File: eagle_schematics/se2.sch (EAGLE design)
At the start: 8 parts, among them J1 MAGJACK-NOLABELS

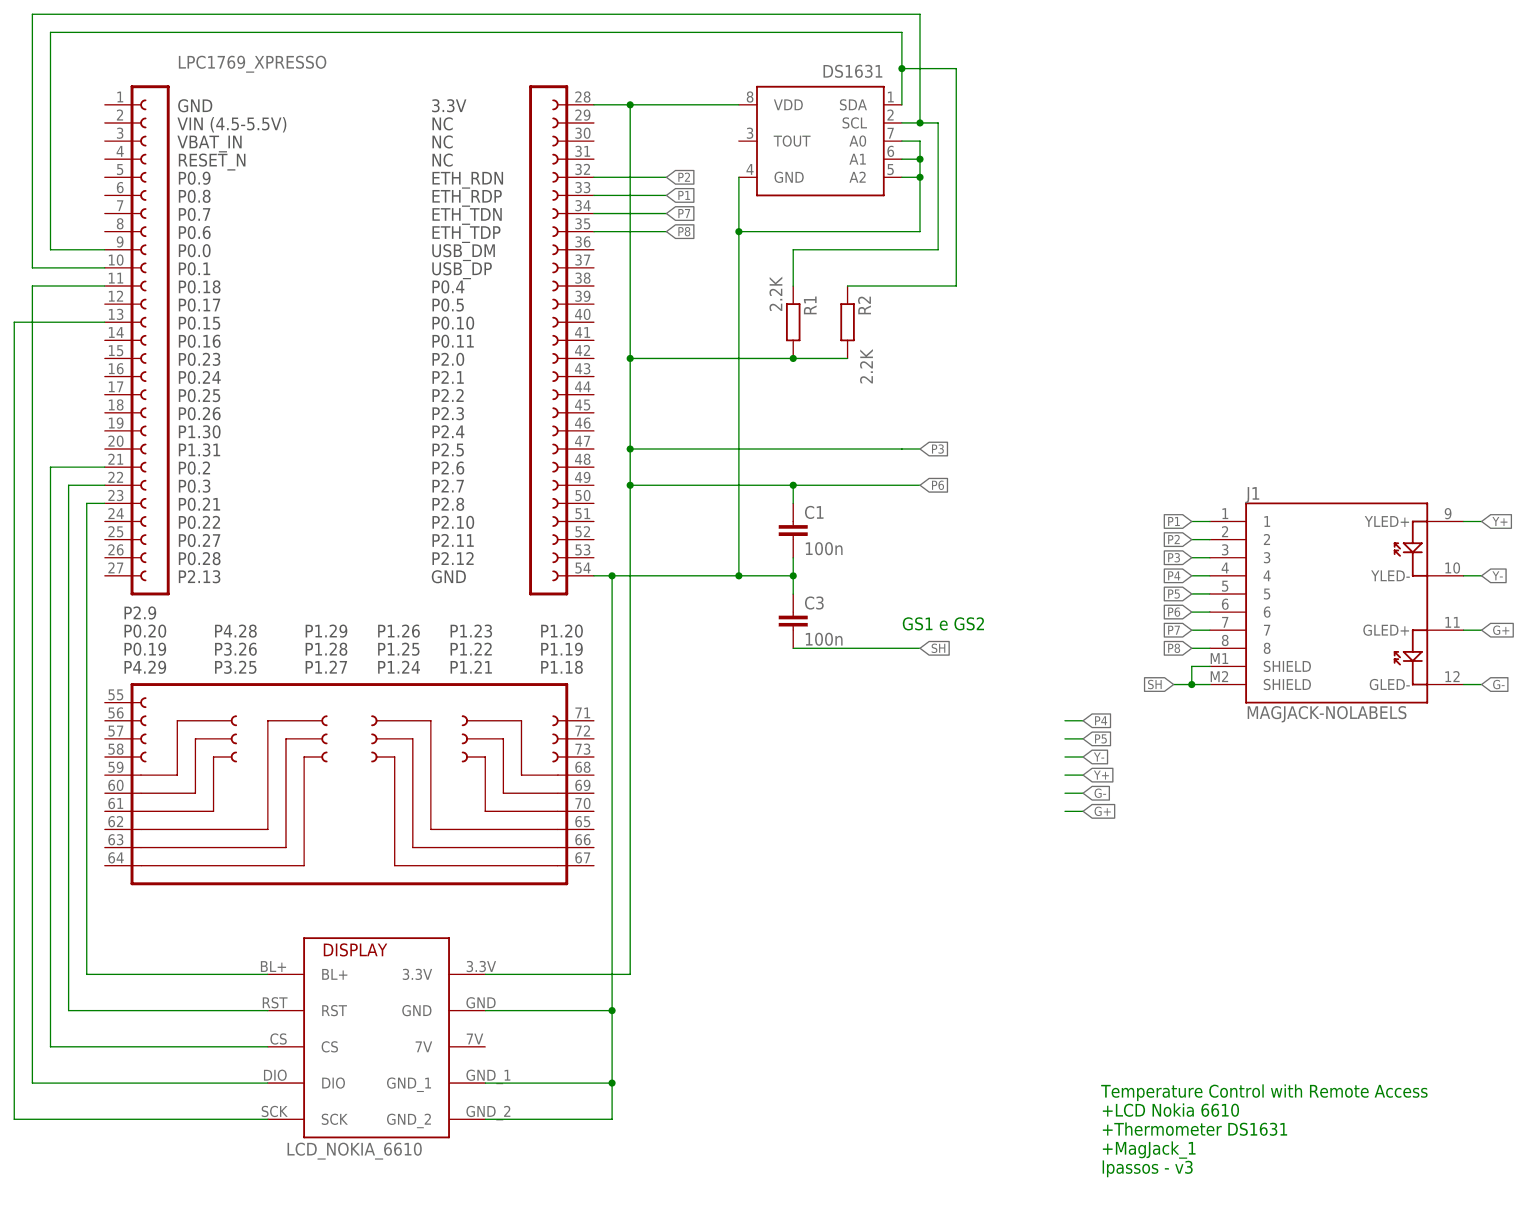
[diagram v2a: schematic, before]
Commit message: led schematic added
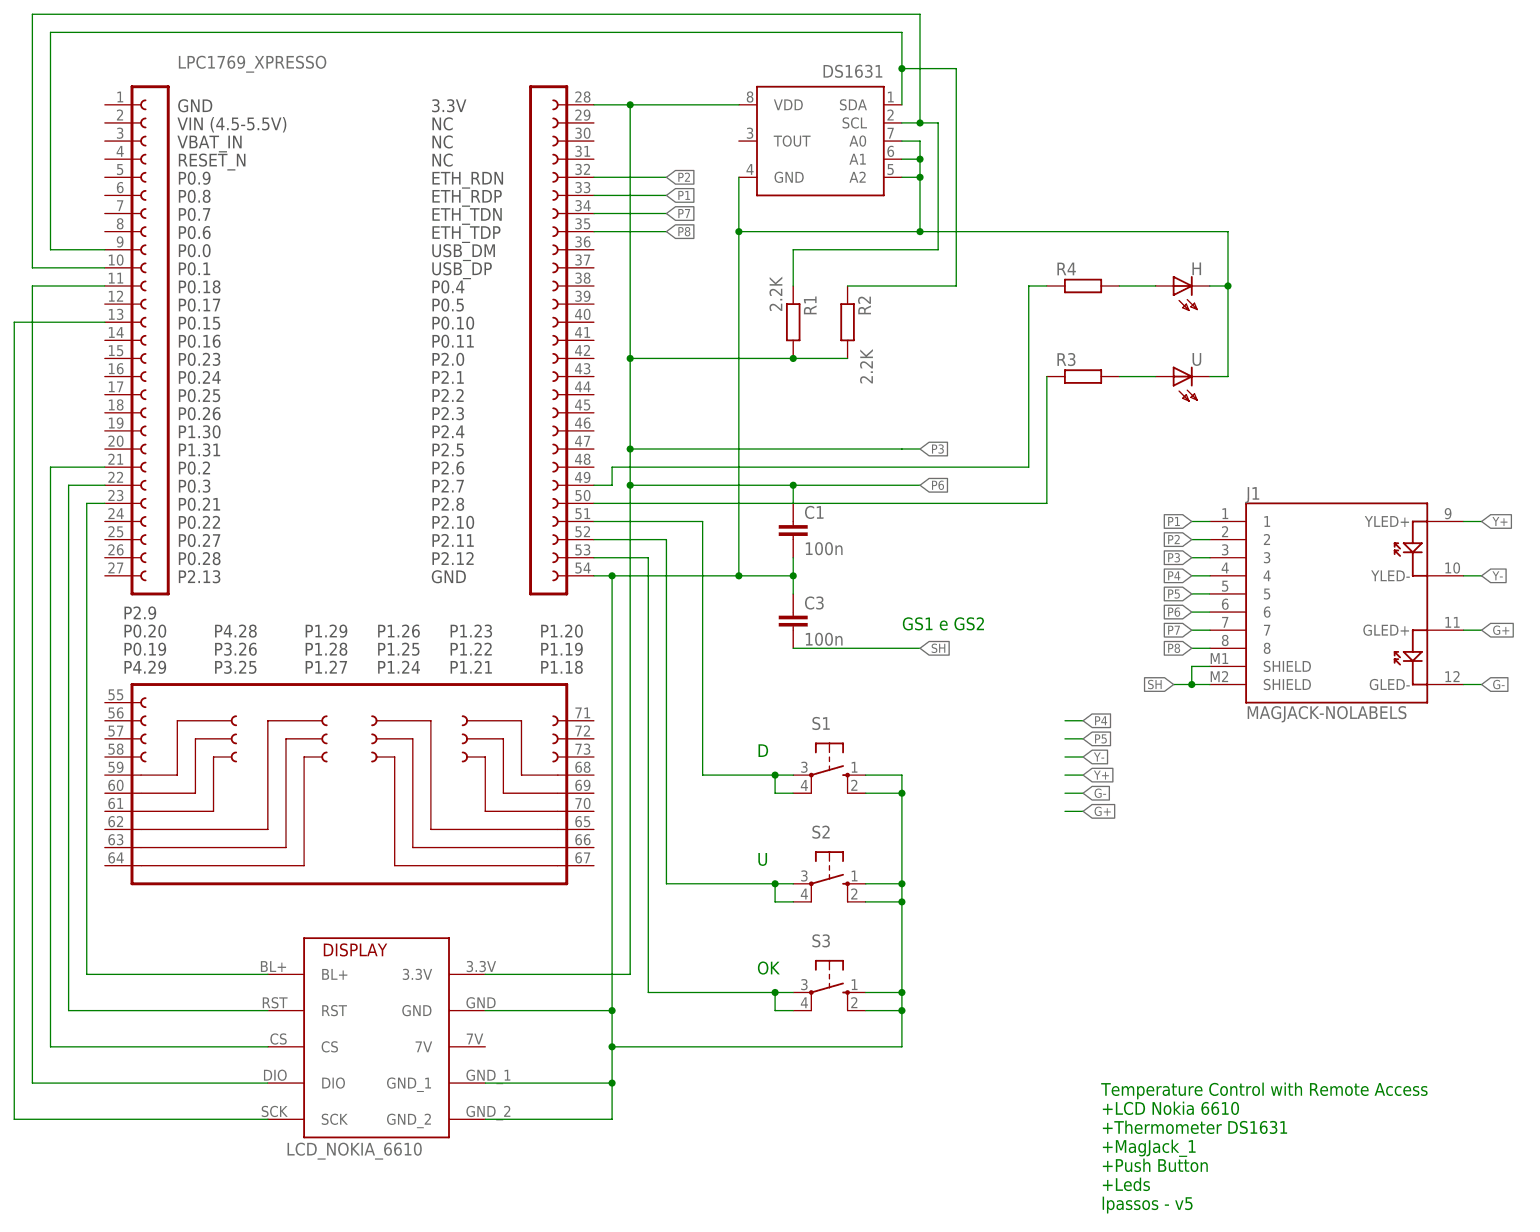
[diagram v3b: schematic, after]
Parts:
- added H, U: HLMP6, display-hp:HLMP6
- added R3, R4: (no value), eagle-ltspice:R
- added S1, S2, S3: (no value), switch-omron:10-XX
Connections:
- new net N$1: LPC1769_XPRESSO.51, S1.P, S1.P1
- new net N$12: LPC1769_XPRESSO.52, S2.P, S2.P1
- new net N$13: R3.2, U.A
- new net N$14: LPC1769_XPRESSO.50, R3.1
- new net N$15: LPC1769_XPRESSO.49, R4.1
- new net N$2: LPC1769_XPRESSO.53, S3.P, S3.P1
- new net N$3: H.A, R4.2
- net N$9: now also H.K, S1.S, S1.S1, S2.S, S2.S1, S3.S, S3.S1, U.K
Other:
- note added: "D"
- note added: "OK"
- note added: "Temperature Control with Remote Access +LCD Nokia 6610 +Thermometer DS1631 +MagJack_1 +Push Button +Leds lpassos - v5"
- note added: "U"
- note removed: "Temperature Control with Remote Access +LCD Nokia 6610 +Thermometer DS1631 +MagJack_1 lpassos - v3"
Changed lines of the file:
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@@
 <setting verticaltext="up"/>
 </settings>
-<grid distance="0.1" unitdist="inch" unit="inch" style="lines" multiple="1" display="no" altdistance="0.01" altunitdist="inch" altunit="inch"/>
+<grid distance="0.1" unitdist="inch" unit="inch" style="lines" multiple="1" display="yes" altdistance="0.01" altunitdist="inch" altunit="inch"/>
 <layers>
 <layer number="1" name="Top" color="4" fill="1" visible="no" active="no"/>
@@
 <part name="C1" library="capacitor-wima" deviceset="C" device="2,5-3" value="100n"/>
 <part name="C3" library="capacitor-wima" deviceset="C" device="2,5-3" value="100n"/>
+<part name="S1" library="switch-omron" deviceset="10-XX" device=""/>
+<part name="S2" library="switch-omron" deviceset="10-XX" device=""/>
+<part name="S3" library="switch-omron" deviceset="10-XX" device=""/>
+<part name="R3" library="eagle-ltspice" deviceset="R" device=""/>
+<part name="R4" library="eagle-ltspice" deviceset="R" device=""/>
+<part name="H" library="display-hp" deviceset="HLMP6" device="" value=""/>
+<part name="U" library="display-hp" deviceset="HLMP6" device="" value=""/>
 </parts>
 <sheets>
 <sheet>
 <plain>
-<text x="182.88" y="93.98" size="1.778" layer="91">Temperature Control with Remote Access
+<text x="182.88" y="88.9" size="1.778" layer="91">Temperature Control with Remote Access
 +LCD Nokia 6610
 +Thermometer DS1631
 +MagJack_1
-lpassos - v3</text>
++Push Button
++Leds
+lpassos - v5</text>
 <text x="154.94" y="170.18" size="1.778" layer="91">GS1 e GS2</text>
+<text x="134.62" y="121.92" size="1.778" layer="91">OK</text>
+<text x="134.62" y="137.16" size="1.778" layer="91">U</text>
+<text x="134.62" y="152.4" size="1.778" layer="91">D</text>
 </plain>
 <instances>
@@
 <instance part="C1" gate="G$1" x="139.7" y="185.42"/>
 <instance part="C3" gate="G$1" x="139.7" y="172.72"/>
+<instance part="S1" gate="1" x="144.78" y="149.86" rot="R270"/>
+<instance part="S2" gate="1" x="144.78" y="134.62" rot="R270"/>
+<instance part="S3" gate="1" x="144.78" y="119.38" rot="R270"/>
+<instance part="R3" gate="G$1" x="180.34" y="205.74"/>
+<instance part="R4" gate="G$1" x="180.34" y="218.44"/>
+<instance part="H" gate="A" x="195.58" y="218.44" rot="R90"/>
+<instance part="U" gate="A" x="195.58" y="205.74" rot="R90"/>
 </instances>
 <busses>
@@
 <pinref part="DISPLAY" gate="G$1" pin="GND_1"/>
 <wire x1="96.52" y1="106.68" x2="114.3" y2="106.68" width="0.1524" layer="91"/>
-<wire x1="114.3" y1="106.68" x2="114.3" y2="116.84" width="0.1524" layer="91"/>
+<wire x1="114.3" y1="106.68" x2="114.3" y2="111.76" width="0.1524" layer="91"/>
 <pinref part="DISPLAY" gate="G$1" pin="GND_2"/>
+<wire x1="114.3" y1="111.76" x2="114.3" y2="116.84" width="0.1524" layer="91"/>
 <wire x1="96.52" y1="101.6" x2="114.3" y2="101.6" width="0.1524" layer="91"/>
 <wire x1="114.3" y1="101.6" x2="114.3" y2="106.68" width="0.1524" layer="91"/>
@@
 <pinref part="C3" gate="G$1" pin="1"/>
 <wire x1="139.7" y1="175.26" x2="139.7" y2="177.8" width="0.1524" layer="91"/>
+<wire x1="154.94" y1="147.32" x2="154.94" y2="134.62" width="0.1524" layer="91"/>
+<wire x1="154.94" y1="134.62" x2="154.94" y2="132.08" width="0.1524" layer="91"/>
+<wire x1="154.94" y1="132.08" x2="154.94" y2="119.38" width="0.1524" layer="91"/>
+<wire x1="154.94" y1="119.38" x2="154.94" y2="116.84" width="0.1524" layer="91"/>
+<wire x1="154.94" y1="116.84" x2="154.94" y2="111.76" width="0.1524" layer="91"/>
+<wire x1="154.94" y1="111.76" x2="114.3" y2="111.76" width="0.1524" layer="91"/>
+<junction x="114.3" y="111.76"/>
+<pinref part="S1" gate="1" pin="S1"/>
+<wire x1="149.86" y1="147.32" x2="154.94" y2="147.32" width="0.1524" layer="91"/>
+<pinref part="S3" gate="1" pin="S1"/>
+<wire x1="149.86" y1="116.84" x2="154.94" y2="116.84" width="0.1524" layer="91"/>
+<junction x="154.94" y="116.84"/>
+<pinref part="S2" gate="1" pin="S1"/>
+<wire x1="149.86" y1="132.08" x2="154.94" y2="132.08" width="0.1524" layer="91"/>
+<junction x="154.94" y="132.08"/>
+<pinref part="S1" gate="1" pin="S"/>
+<wire x1="149.86" y1="149.86" x2="154.94" y2="149.86" width="0.1524" layer="91"/>
+<wire x1="154.94" y1="149.86" x2="154.94" y2="147.32" width="0.1524" layer="91"/>
+<pinref part="S2" gate="1" pin="S"/>
+<wire x1="149.86" y1="134.62" x2="154.94" y2="134.62" width="0.1524" layer="91"/>
+<pinref part="S3" gate="1" pin="S"/>
+<wire x1="149.86" y1="119.38" x2="154.94" y2="119.38" width="0.1524" layer="91"/>
+<junction x="154.94" y="147.32"/>
+<junction x="154.94" y="134.62"/>
+<junction x="154.94" y="119.38"/>
+<pinref part="H" gate="A" pin="K"/>
+<wire x1="198.12" y1="218.44" x2="200.66" y2="218.44" width="0.1524" layer="91"/>
+<wire x1="200.66" y1="218.44" x2="200.66" y2="205.74" width="0.1524" layer="91"/>
+<pinref part="U" gate="A" pin="K"/>
+<wire x1="200.66" y1="205.74" x2="198.12" y2="205.74" width="0.1524" layer="91"/>
+<wire x1="157.48" y1="226.06" x2="200.66" y2="226.06" width="0.1524" layer="91"/>
+<wire x1="200.66" y1="226.06" x2="200.66" y2="218.44" width="0.1524" layer="91"/>
+<junction x="200.66" y="218.44"/>
+<junction x="157.48" y="226.06"/>
 </segment>
 </net>
@@
 </segment>
 </net>
+<net name="N$2" class="0">
+<segment>
+<pinref part="LPC1769_XPRESSO" gate="G$1" pin="53"/>
+<wire x1="111.76" y1="180.34" x2="119.38" y2="180.34" width="0.1524" layer="91"/>
+<wire x1="119.38" y1="180.34" x2="119.38" y2="119.38" width="0.1524" layer="91"/>
+<pinref part="S3" gate="1" pin="P"/>
+<wire x1="119.38" y1="119.38" x2="137.16" y2="119.38" width="0.1524" layer="91"/>
+<pinref part="S3" gate="1" pin="P1"/>
+<wire x1="137.16" y1="119.38" x2="139.7" y2="119.38" width="0.1524" layer="91"/>
+<wire x1="139.7" y1="116.84" x2="137.16" y2="116.84" width="0.1524" layer="91"/>
+<wire x1="137.16" y1="116.84" x2="137.16" y2="119.38" width="0.1524" layer="91"/>
+<junction x="137.16" y="119.38"/>
+</segment>
+</net>
+<net name="N$12" class="0">
+<segment>
+<pinref part="LPC1769_XPRESSO" gate="G$1" pin="52"/>
+<wire x1="111.76" y1="182.88" x2="121.92" y2="182.88" width="0.1524" layer="91"/>
+<wire x1="121.92" y1="182.88" x2="121.92" y2="134.62" width="0.1524" layer="91"/>
+<pinref part="S2" gate="1" pin="P"/>
+<wire x1="121.92" y1="134.62" x2="137.16" y2="134.62" width="0.1524" layer="91"/>
+<pinref part="S2" gate="1" pin="P1"/>
+<wire x1="137.16" y1="134.62" x2="139.7" y2="134.62" width="0.1524" layer="91"/>
+<wire x1="139.7" y1="132.08" x2="137.16" y2="132.08" width="0.1524" layer="91"/>
+<wire x1="137.16" y1="132.08" x2="137.16" y2="134.62" width="0.1524" layer="91"/>
+<junction x="137.16" y="134.62"/>
+</segment>
+</net>
+<net name="N$1" class="0">
+<segment>
+<pinref part="LPC1769_XPRESSO" gate="G$1" pin="51"/>
+<wire x1="111.76" y1="185.42" x2="127" y2="185.42" width="0.1524" layer="91"/>
+<wire x1="127" y1="185.42" x2="127" y2="149.86" width="0.1524" layer="91"/>
+<pinref part="S1" gate="1" pin="P"/>
+<wire x1="127" y1="149.86" x2="137.16" y2="149.86" width="0.1524" layer="91"/>
+<pinref part="S1" gate="1" pin="P1"/>
+<wire x1="137.16" y1="149.86" x2="139.7" y2="149.86" width="0.1524" layer="91"/>
+<wire x1="139.7" y1="147.32" x2="137.16" y2="147.32" width="0.1524" layer="91"/>
+<wire x1="137.16" y1="147.32" x2="137.16" y2="149.86" width="0.1524" layer="91"/>
+<junction x="137.16" y="149.86"/>
+</segment>
+</net>
+<net name="N$3" class="0">
+<segment>
+<pinref part="R4" gate="G$1" pin="2"/>
+<pinref part="H" gate="A" pin="A"/>
+<wire x1="185.42" y1="218.44" x2="190.5" y2="218.44" width="0.1524" layer="91"/>
+</segment>
+</net>
+<net name="N$13" class="0">
+<segment>
+<pinref part="R3" gate="G$1" pin="2"/>
+<pinref part="U" gate="A" pin="A"/>
+<wire x1="185.42" y1="205.74" x2="190.5" y2="205.74" width="0.1524" layer="91"/>
+</segment>
+</net>
+<net name="N$14" class="0">
+<segment>
+<pinref part="LPC1769_XPRESSO" gate="G$1" pin="50"/>
+<pinref part="R3" gate="G$1" pin="1"/>
+<wire x1="111.76" y1="187.96" x2="175.26" y2="187.96" width="0.1524" layer="91"/>
+<wire x1="175.26" y1="187.96" x2="175.26" y2="205.74" width="0.1524" layer="91"/>
+</segment>
+</net>
+<net name="N$15" class="0">
+<segment>
+<pinref part="LPC1769_XPRESSO" gate="G$1" pin="49"/>
+<wire x1="111.76" y1="190.5" x2="114.3" y2="190.5" width="0.1524" layer="91"/>
+<wire x1="114.3" y1="190.5" x2="114.3" y2="193.04" width="0.1524" layer="91"/>
+<wire x1="114.3" y1="193.04" x2="172.72" y2="193.04" width="0.1524" layer="91"/>
+<wire x1="172.72" y1="193.04" x2="172.72" y2="218.44" width="0.1524" layer="91"/>
+<pinref part="R4" gate="G$1" pin="1"/>
+<wire x1="172.72" y1="218.44" x2="175.26" y2="218.44" width="0.1524" layer="91"/>
+</segment>
+</net>
